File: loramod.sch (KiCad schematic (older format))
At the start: 79 parts, among them P1 CONN_02X08, P2 ANT, U1 VCTCXO, U2 LD3985G30R, U3 SX1276, U4 PE42421, U5 MAAL-010704, U6 MMZ09312BT1

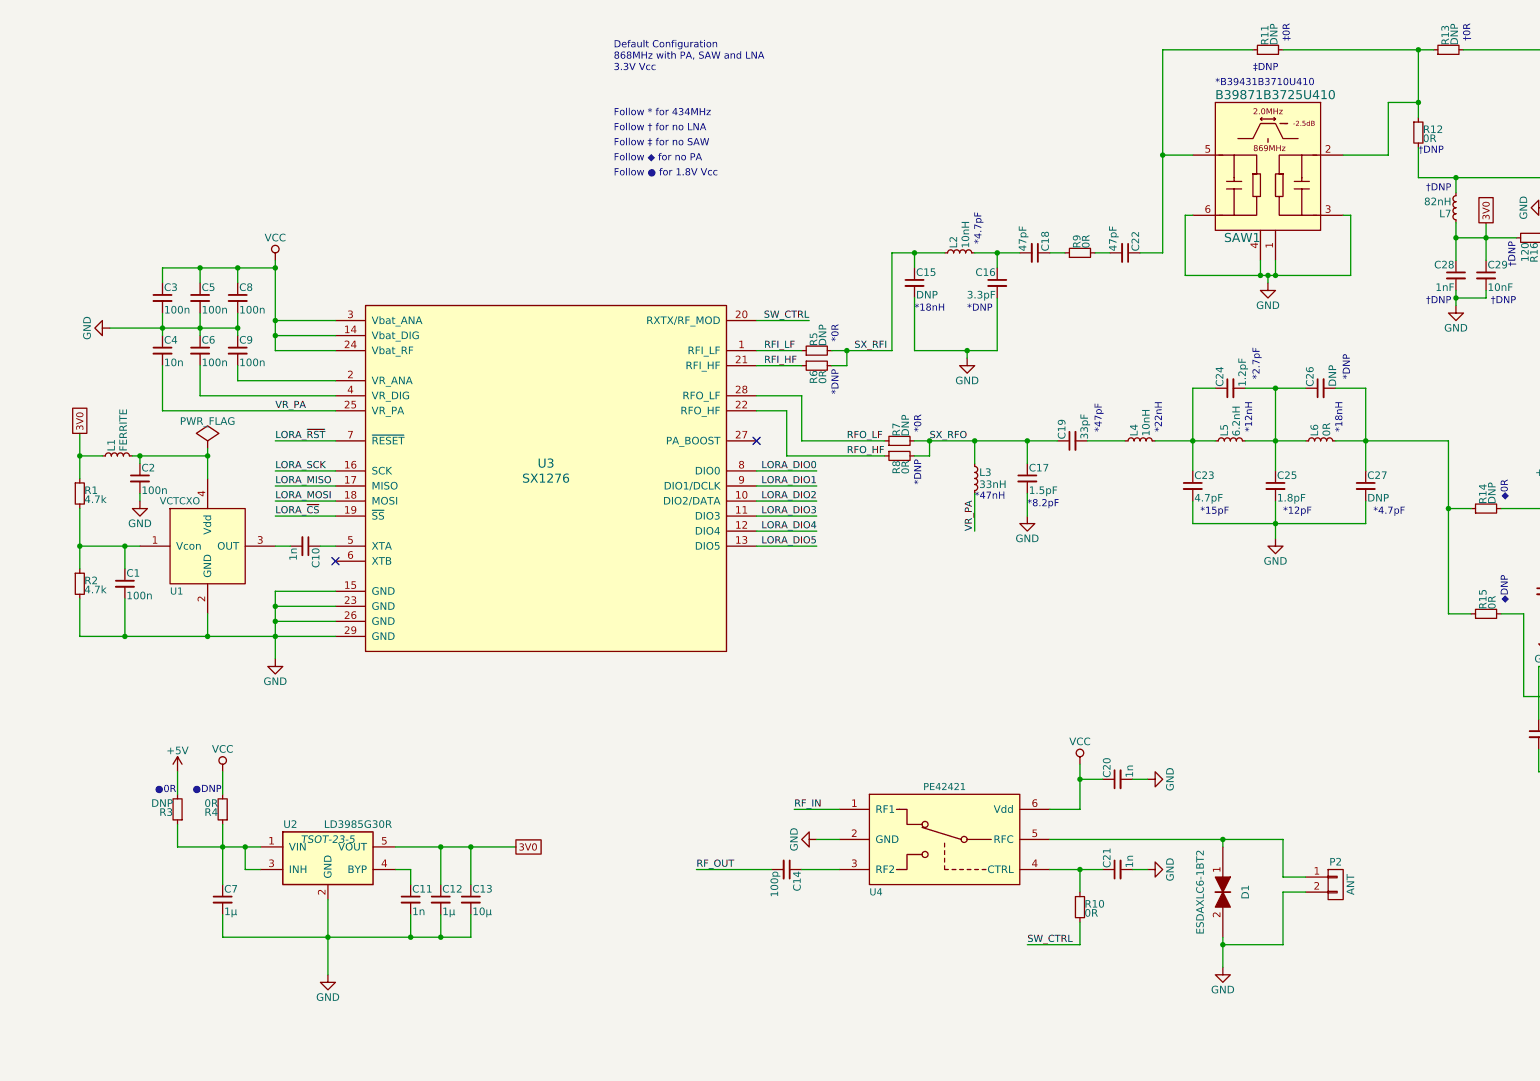
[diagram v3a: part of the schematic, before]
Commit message: Start placing PCB parts
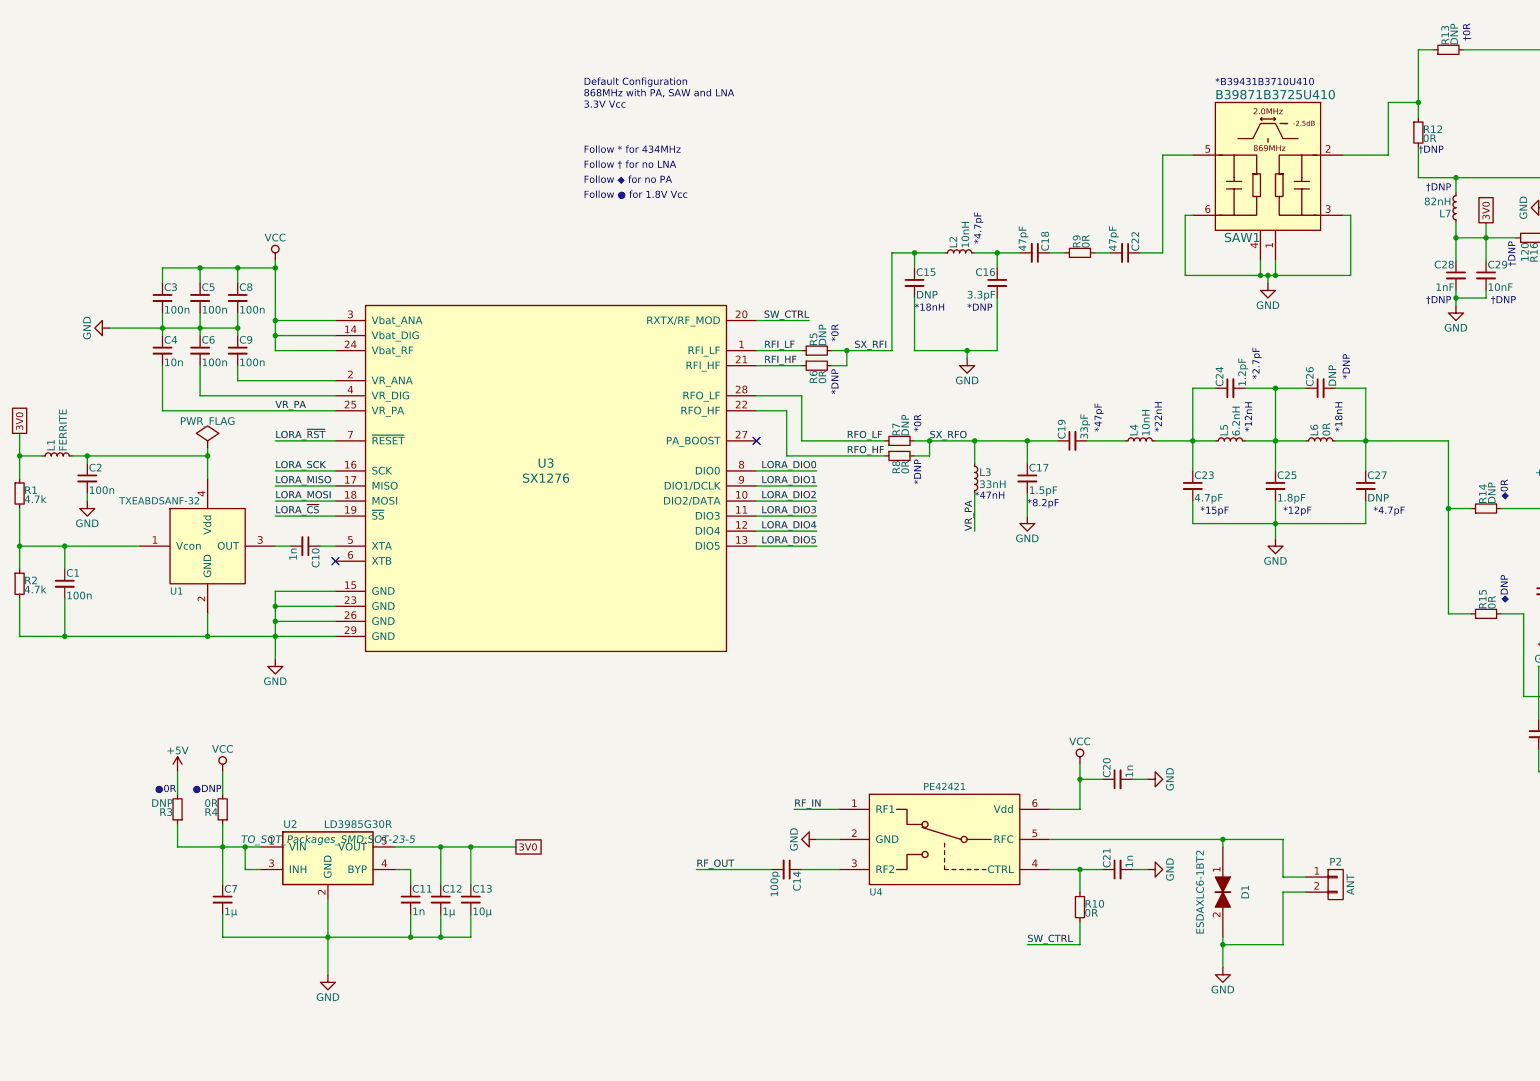
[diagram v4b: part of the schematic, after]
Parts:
- removed R11: DNP, symbol R_Small
- C1, C10, C11, C14, C15, C16, C17, C18, C19, C2, C20, C21, C22, C23, C24, C25, C26, C27, C28, C29, C3, C30, C31, C32, C33, C34, C36, C4, C5, C6, C8, C9, D1: footprint (none) -> Capacitors_SMD:C_0402
- C12: footprint (none) -> Capacitors_SMD:C_0603
- C13, C35: footprint (none) -> Capacitors_SMD:C_0805
- C7: footprint (none) -> Capacitors_SMD:C_0603_HandSoldering
- L1, L10, L11, L12, L2, L3, L4, L5, L6, L7, L8, L9, R1, R10, R12, R13, R14, R15, R16, R17, R18, R19, R2, R20, R21, R3, R4, R5, R6, R7, R8, R9: footprint (none) -> Resistors_SMD:R_0402
- P1: footprint (none) -> Pin_Headers:Pin_Header_Straight_2x08_Pitch2.00mm
- P2: footprint (none) -> Custom Parts - global:RFcon
- SAW1: footprint (none) -> Custom Parts - global:SAW-DCC6C
- U1: value VCTCXO -> TXEABDSANF-32; footprint (none) -> Custom Parts - global:TCXO-WT325
- U2: footprint TSOT-23-5 -> TO_SOT_Packages_SMD:SOT-23-5
- U3: footprint (none) -> Housings_DFN_QFN:QFN-28-1EP_6x6mm_Pitch0.65mm
- U4, U5: footprint (none) -> TO_SOT_Packages_SMD:SC-70-6_Handsoldering
- U6: footprint (none) -> Housings_DFN_QFN:QFN-12-1EP_3x3mm_Pitch0.5mm
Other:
- note removed: "Follow ‡ for no SAW"
- note removed: "‡0R"
- note removed: "‡DNP"
- moved on the sheet: C1, C2, L1, R1, R2

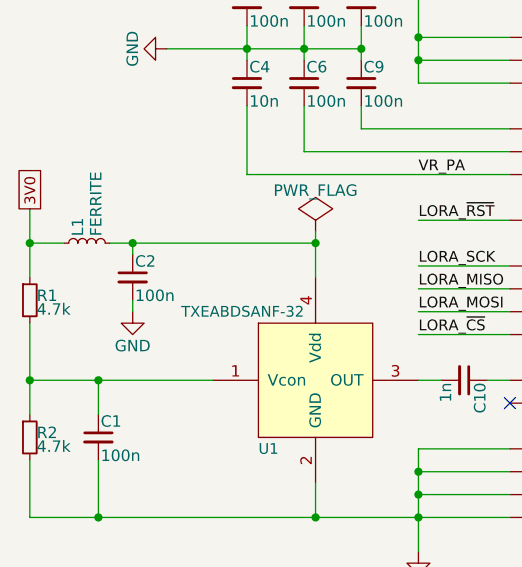
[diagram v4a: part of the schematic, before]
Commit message: PCB part placement done
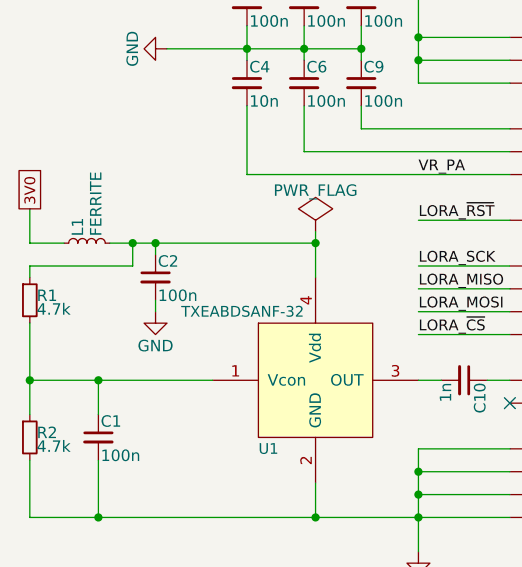
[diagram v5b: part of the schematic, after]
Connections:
- net 3V0: no longer R1.1
- net at C2.1, L1.2, U1.4 (Vdd): now also R1.1
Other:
- moved on the sheet: C2
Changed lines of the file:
@@
 L C_Small C2
 U 1 1 57D91397
-P 1450 3500
-F 0 "C2" H 1460 3570 50  0000 L CNN
-F 1 "100n" H 1460 3420 50  0000 L CNN
-F 2 "Capacitors_SMD:C_0402" H 1450 3500 50  0001 C CNN
-F 3 "" H 1450 3500 50  0000 C CNN
-	1    1450 3500
+P 1550 3500
+F 0 "C2" H 1560 3570 50  0000 L CNN
+F 1 "100n" H 1560 3420 50  0000 L CNN
+F 2 "Capacitors_SMD:C_0402" H 1550 3500 50  0001 C CNN
+F 3 "" H 1550 3500 50  0000 C CNN
+	1    1550 3500
 	1    0    0    -1
 $EndComp
@@
 L GND #PWR04
 U 1 1 57D914E3
-P 1450 3650
-F 0 "#PWR04" H 1450 3400 50  0001 C CNN
-F 1 "GND" H 1450 3500 50  0000 C CNN
-F 2 "" H 1450 3650 50  0000 C CNN
-F 3 "" H 1450 3650 50  0000 C CNN
-	1    1450 3650
+P 1550 3650
+F 0 "#PWR04" H 1550 3400 50  0001 C CNN
+F 1 "GND" H 1550 3500 50  0000 C CNN
+F 2 "" H 1550 3650 50  0000 C CNN
+F 3 "" H 1550 3650 50  0000 C CNN
+	1    1550 3650
 	1    0    0    -1
 $EndComp
@@
 Connection ~ 2250 3350
 Wire Wire Line
-	1450 3350 1450 3400
-Connection ~ 1450 3350
-Wire Wire Line
-	1450 3650 1450 3600
-Wire Wire Line
-	1000 3200 1000 3500
+	1550 3350 1550 3400
+Connection ~ 1550 3350
+Wire Wire Line
+	1550 3650 1550 3600
 Wire Wire Line
 	1000 3350 1150 3350
@@
 	1300 4100 1300 3950
 Connection ~ 1300 3950
-Connection ~ 1000 3350
 Wire Wire Line
 	1000 4300 1000 4550
@@
 Wire Wire Line
 	10300 650  10400 650
+Wire Wire Line
+	1450 3350 1450 3450
+Wire Wire Line
+	1450 3450 1000 3450
+Wire Wire Line
+	1000 3450 1000 3500
+Connection ~ 1450 3350
+Wire Wire Line
+	1000 3350 1000 3200
 $EndSCHEMATC
